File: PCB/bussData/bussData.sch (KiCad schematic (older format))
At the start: 7 parts

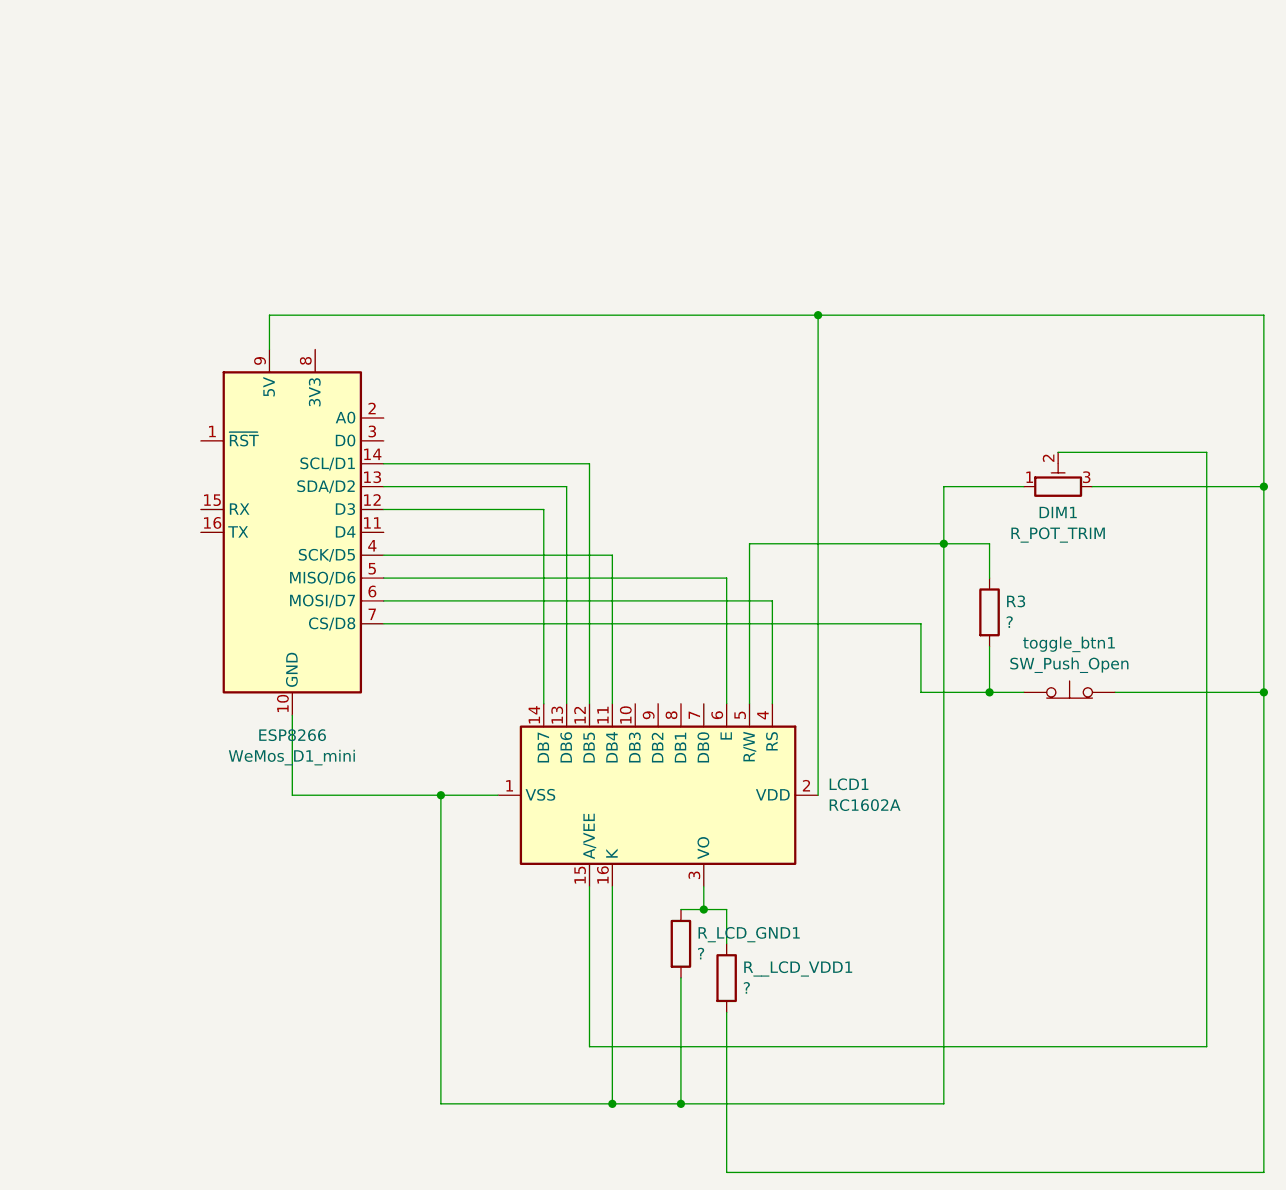
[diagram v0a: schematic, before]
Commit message: updated the PCB
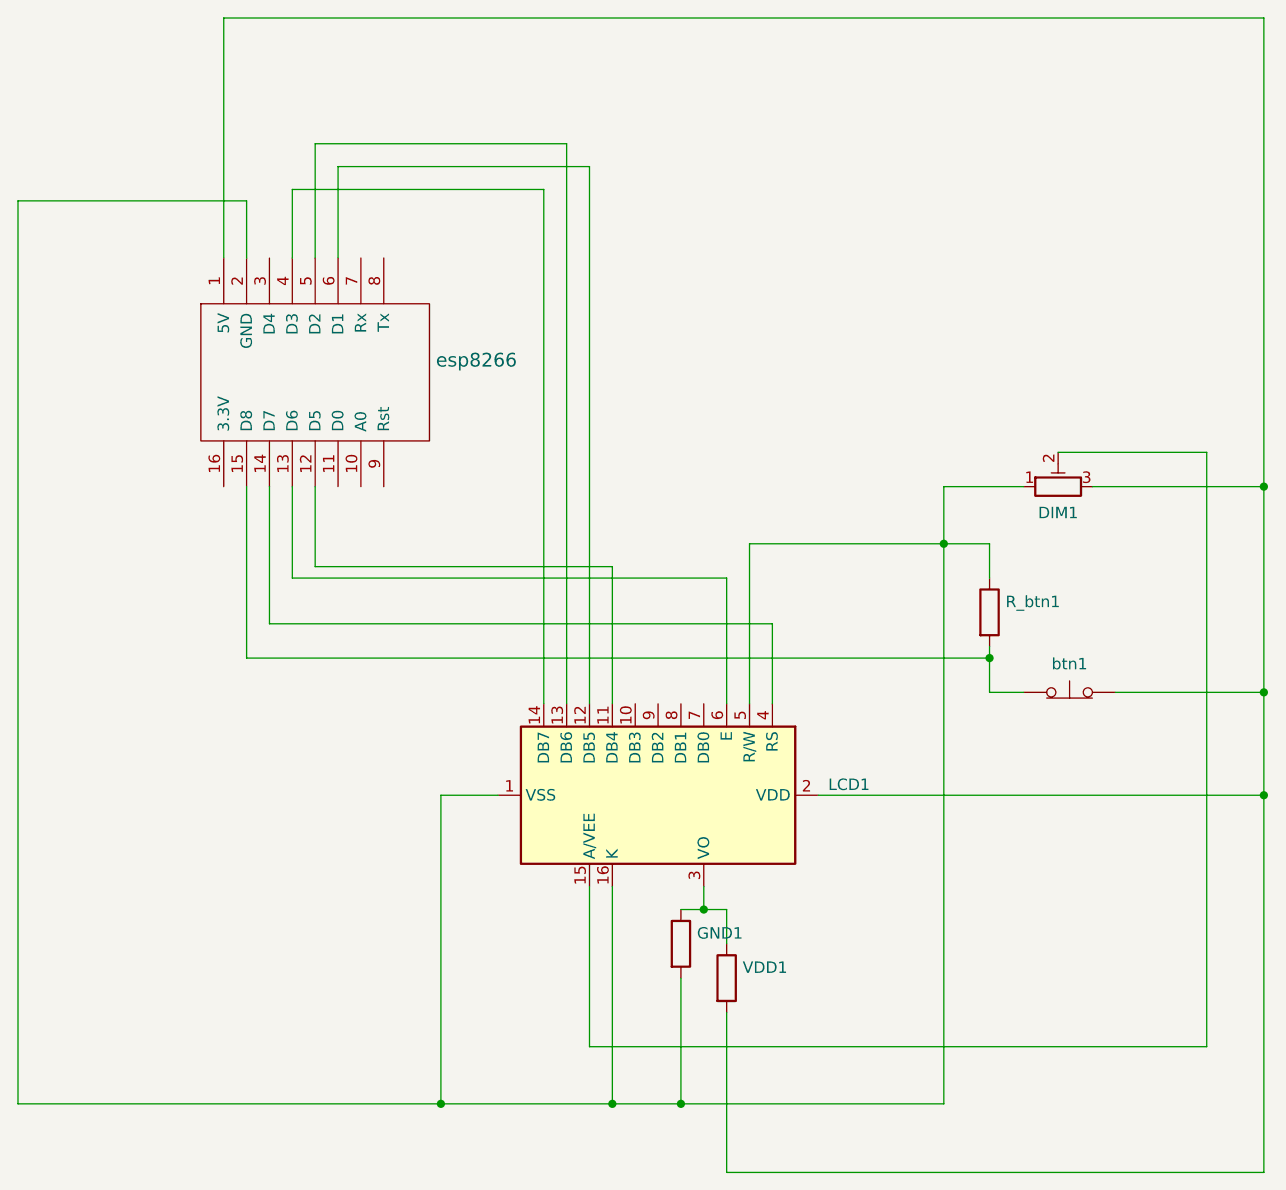
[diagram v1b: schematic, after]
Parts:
- removed ESP8266: WeMos_D1_mini, Module:WEMOS_D1_mini_light, symbol MCU_Module:WeMos_D1_mini
- removed toggle_btn1: SW_Push_Open, Connector_PinSocket_2.00mm:PinSocket_1x02_P2.00mm_Vertical, symbol Switch:SW_Push_Open
- added btn1: SW_Push_Open, Switch_Keyboard_Cherry_MX:SW_Cherry_MX_PCB_1.00u, symbol Switch:SW_Push_Open
- added esp8266: WeMos_mini, Module:D1_mini_board, symbol wemos_mini:WeMos_mini
- LCD1: footprint Display:RC1602A -> Display:WC1602A
- renumbered R_LCD_GND1 to GND1, R3 to R_btn1, R__LCD_VDD1 to VDD1
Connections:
- net at DIM1.1, GND1.2, LCD1.1 (VSS)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: now also esp8266.2 (GND)
- net at LCD1.14 (DB7): now also esp8266.4 (D3)
- net at LCD1.13 (DB6): now also esp8266.5 (D2)
- net at LCD1.12 (DB5): now also esp8266.6 (D1)
- net at LCD1.11 (DB4): now also esp8266.12 (D5)
- net at LCD1.6 (E): now also esp8266.13 (D6)
- net at LCD1.4 (RS): now also esp8266.14 (D7)
- net at R_btn1.2: now also btn1.1 (A), esp8266.15 (D8)
- net at DIM1.3, LCD1.2 (VDD), VDD1.2: now also btn1.2 (B), esp8266.1 (5V)
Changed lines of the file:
@@
 P 4100 4300
 F 0 "LCD1" V 4054 5044 50  0000 L CNN
-F 1 "RC1602A" V 4145 5044 50  0000 L CNN
-F 2 "Display:RC1602A" H 4200 3500 50  0001 C CNN
+F 1 "RC1602A" V 4145 5044 50  0001 L CNN
+F 2 "Display:WC1602A" H 4200 3500 50  0001 C CNN
 F 3 "http://www.raystar-optronics.com/down.php?ProID=18" H 4200 4200 50  0001 C CNN
 	1    4100 4300
@@
 $EndComp
 $Comp
-L Switch:SW_Push_Open toggle_btn1
-U 1 1 6164529D
-P 5900 3850
-F 0 "toggle_btn1" H 5900 4065 50  0000 C CNN
-F 1 "SW_Push_Open" H 5900 3974 50  0000 C CNN
-F 2 "Connector_PinSocket_2.00mm:PinSocket_1x02_P2.00mm_Vertical" H 5900 4050 50  0001 C CNN
-F 3 "~" H 5900 4050 50  0001 C CNN
-	1    5900 3850
-	1    0    0    -1
-$EndComp
-$Comp
-L Device:R R_LCD_GND1
+L Device:R GND1
 U 1 1 6164578F
 P 4200 4950
-F 0 "R_LCD_GND1" H 4270 4996 50  0000 L CNN
-F 1 "?" H 4270 4905 50  0000 L CNN
+F 0 "GND1" H 4270 4996 50  0000 L CNN
+F 1 "?" H 4270 4905 50  0001 L CNN
 F 2 "Resistor_THT:R_Axial_DIN0207_L6.3mm_D2.5mm_P10.16mm_Horizontal" V 4130 4950 50  0001 C CNN
 F 3 "~" H 4200 4950 50  0001 C CNN
@@
 $EndComp
 $Comp
-L Device:R R__LCD_VDD1
+L Device:R VDD1
 U 1 1 61645FE6
 P 4400 5100
-F 0 "R__LCD_VDD1" H 4470 5146 50  0000 L CNN
-F 1 "?" H 4470 5055 50  0000 L CNN
+F 0 "VDD1" H 4470 5146 50  0000 L CNN
+F 1 "?" H 4470 5055 50  0001 L CNN
 F 2 "Resistor_THT:R_Axial_DIN0207_L6.3mm_D2.5mm_P10.16mm_Horizontal" V 4330 5100 50  0001 C CNN
 F 3 "~" H 4400 5100 50  0001 C CNN
@@
 $EndComp
 $Comp
-L Device:R R3
+L Device:R R_btn1
 U 1 1 61646194
 P 5550 3500
-F 0 "R3" H 5620 3546 50  0000 L CNN
-F 1 "?" H 5620 3455 50  0000 L CNN
+F 0 "R_btn1" H 5620 3546 50  0000 L CNN
+F 1 "?" H 5620 3455 50  0001 L CNN
 F 2 "Resistor_THT:R_Axial_DIN0207_L6.3mm_D2.5mm_P10.16mm_Horizontal" V 5480 3500 50  0001 C CNN
 F 3 "~" H 5550 3500 50  0001 C CNN
@@
 P 5850 2950
 F 0 "DIM1" V 5735 2950 50  0000 C CNN
-F 1 "R_POT_TRIM" V 5644 2950 50  0000 C CNN
+F 1 "R_POT_TRIM" V 5644 2950 50  0001 C CNN
 F 2 "Potentiometer_THT:Potentiometer_Vishay_T73YP_Vertical" H 5850 2950 50  0001 C CNN
 F 3 "~" H 5850 2950 50  0001 C CNN
@@
 $EndComp
 Wire Wire Line
-	3800 2850 3800 3900
-Wire Wire Line
-	2900 2950 3700 2950
-Wire Wire Line
-	3700 2950 3700 3900
-Wire Wire Line
-	3600 3050 3600 3900
-Wire Wire Line
-	3900 3250 3900 3900
-Wire Wire Line
-	2900 3350 4400 3350
-Wire Wire Line
-	4400 3350 4400 3900
-Wire Wire Line
-	2900 3450 4600 3450
-Wire Wire Line
-	4600 3450 4600 3900
-Wire Wire Line
-	5250 3550 5250 3850
-Wire Wire Line
-	5250 3850 5550 3850
-Wire Wire Line
-	5550 3850 5550 3650
-Connection ~ 5550 3850
+	5550 3850 5550 3700
 Wire Wire Line
 	5550 3850 5700 3850
-Wire Wire Line
-	2900 2850 3800 2850
-Wire Wire Line
-	2900 3050 3600 3050
-Wire Wire Line
-	2900 3250 3900 3250
-Wire Wire Line
-	2900 3550 5250 3550
-$Comp
-L MCU_Module:WeMos_D1_mini ESP8266
-U 1 1 61642F99
-P 2500 3150
-F 0 "ESP8266" H 2500 2261 50  0000 C CNN
-F 1 "WeMos_D1_mini" H 2500 2170 50  0000 C CNN
-F 2 "Module:WEMOS_D1_mini_light" H 2500 2000 50  0001 C CNN
-F 3 "https://wiki.wemos.cc/products:d1:d1_mini#documentation" H 650 2000 50  0001 C CNN
-	1    2500 3150
-	1    0    0    -1
-$EndComp
 Wire Wire Line
 	5850 2800 6500 2800
@@
 Connection ~ 4300 4800
 Wire Wire Line
-	2500 3950 2500 4300
-Wire Wire Line
-	2500 4300 3150 4300
-Wire Wire Line
 	3150 5650 3900 5650
-Connection ~ 3150 4300
 Wire Wire Line
 	3150 4300 3400 4300
@@
 	4500 3200 4500 3900
 Wire Wire Line
-	2400 2350 2400 2200
-Wire Wire Line
-	2400 2200 4800 2200
-Wire Wire Line
-	4800 2200 4800 4300
-Wire Wire Line
-	4800 2200 6750 2200
-Wire Wire Line
 	6750 5950 4400 5950
 Wire Wire Line
 	4400 5950 4400 5250
-Connection ~ 4800 2200
 Wire Wire Line
 	6500 2800 6500 5400
@@
 	6750 3850 6100 3850
 Wire Wire Line
-	6750 3850 6750 5950
+	6750 3850 6750 4300
 Connection ~ 6750 3850
 Wire Wire Line
 	6750 2950 6000 2950
-Wire Wire Line
-	6750 2200 6750 2950
 Wire Wire Line
 	6750 2950 6750 3850
 Connection ~ 6750 2950
+Wire Wire Line
+	2200 1950 2200 900
+Wire Wire Line
+	2200 900  6750 900
+Wire Wire Line
+	6750 900  6750 2950
+Wire Wire Line
+	4800 4300 6750 4300
+Connection ~ 6750 4300
+Wire Wire Line
+	6750 4300 6750 5950
+Wire Wire Line
+	2300 1950 2300 1700
+Wire Wire Line
+	2300 1700 1300 1700
+Wire Wire Line
+	1300 1700 1300 5650
+Wire Wire Line
+	1300 5650 3150 5650
+Connection ~ 3150 5650
+Wire Wire Line
+	2700 1950 2700 1550
+Wire Wire Line
+	2700 1550 3800 1550
+Wire Wire Line
+	3800 1550 3800 3900
+Wire Wire Line
+	2600 1950 2600 1450
+Wire Wire Line
+	2600 1450 3700 1450
+Wire Wire Line
+	3700 1450 3700 3900
+Wire Wire Line
+	2500 1950 2500 1650
+Wire Wire Line
+	2500 1650 3600 1650
+Wire Wire Line
+	3600 1650 3600 3900
+Wire Wire Line
+	2600 2950 2600 3300
+Wire Wire Line
+	2600 3300 3900 3300
+Wire Wire Line
+	3900 3300 3900 3900
+Wire Wire Line
+	2500 2950 2500 3350
+Wire Wire Line
+	2500 3350 4400 3350
+Wire Wire Line
+	4400 3350 4400 3900
+Wire Wire Line
+	2400 2950 2400 3550
+Wire Wire Line
+	2400 3550 4600 3550
+Wire Wire Line
+	4600 3550 4600 3900
+Wire Wire Line
+	5550 3700 2300 3700
+Wire Wire Line
+	2300 3700 2300 2950
+Connection ~ 5550 3700
+Wire Wire Line
+	5550 3700 5550 3650
+$Comp
+L Switch:SW_Push_Open btn1
+U 1 1 616B840E
+P 5900 3850
+F 0 "btn1" H 5900 3974 50  0000 C CNN
+F 1 "SW_Push_Open" H 5900 3974 50  0001 C CNN
+F 2 "Switch_Keyboard_Cherry_MX:SW_Cherry_MX_PCB_1.00u" H 5900 4050 50  0001 C CNN
+F 3 "~" H 5900 4050 50  0001 C CNN
+	1    5900 3850
+	1    0    0    -1
+$EndComp
+$Comp
+L wemos_mini:WeMos_mini esp8266
+U 1 1 61660B12
+P 2550 2450
+F 0 "esp8266" V 2497 1872 60  0000 R CNN
+F 1 "WeMos_mini" V 2603 1872 60  0001 R CNN
+F 2 "Module:D1_mini_board" H 3100 1750 60  0001 C CNN
+F 3 "" H 2550 2981 60  0000 C CNN
+	1    2550 2450
+	0    -1   1    0
+$EndComp
 $EndSCHEMATC
